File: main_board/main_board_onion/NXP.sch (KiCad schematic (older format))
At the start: 17 parts

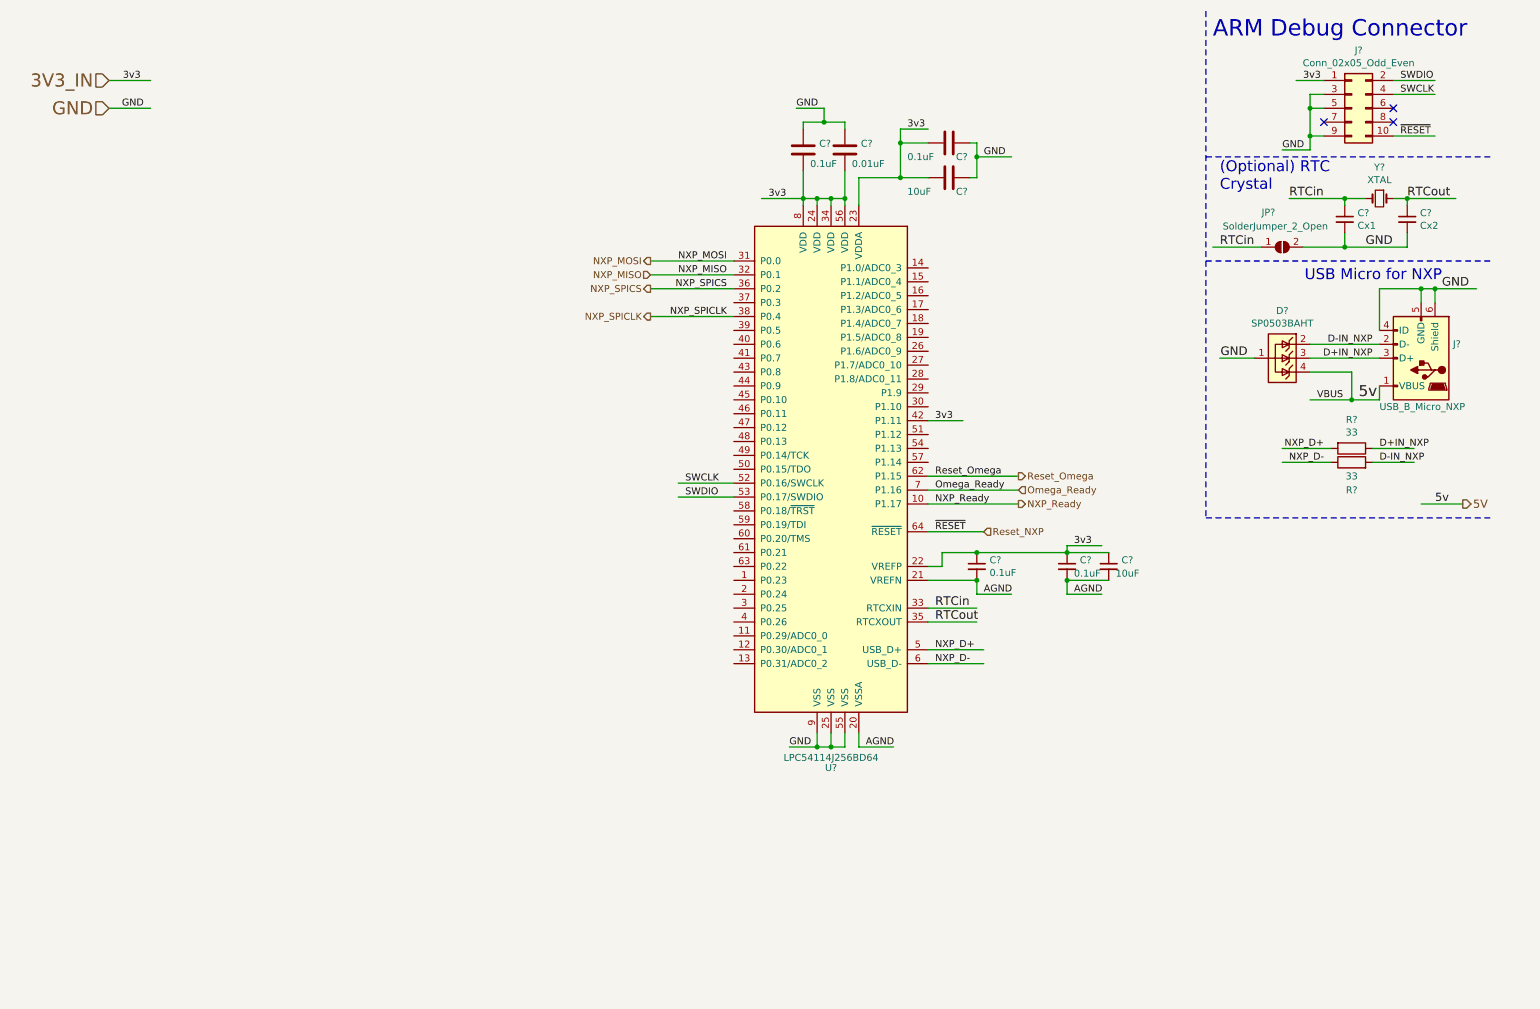
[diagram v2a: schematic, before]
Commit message: Added connectors for sensors
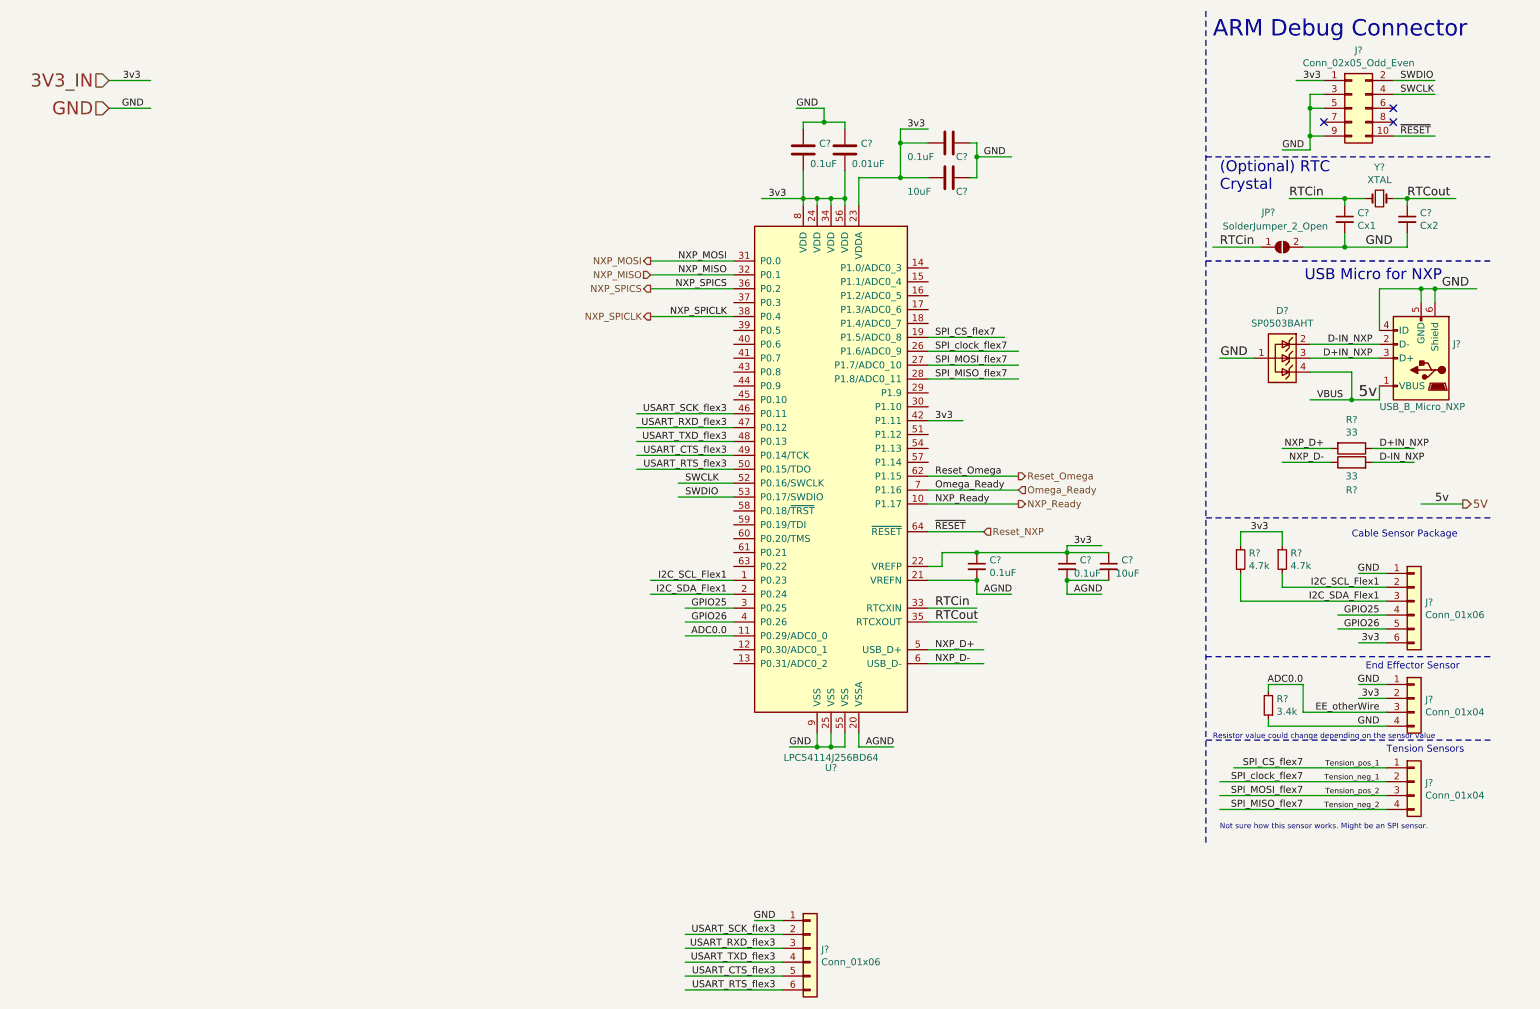
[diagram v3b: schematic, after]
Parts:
- added J? (x2): Conn_01x06, Connector_Molex:Molex_Pico-Lock_504050-0691_1x06-1MP_P1.50mm_Horizontal, symbol Connector_Generic:Conn_01x06
- added J? (x2): Conn_01x04, Connector_Molex:Molex_Pico-Lock_504050-0491_1x04-1MP_P1.50mm_Horizontal, symbol Connector_Generic:Conn_01x04
- added R? (x2): 4.7k, symbol Device:R_Small
- added R?: 3.4k, symbol Device:R_Small
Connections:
- net labels added: ADC0.0, EE_otherWire, GPIO25, GPIO26, I2C_SCL_Flex1, I2C_SDA_Flex1, SPI_CS_flex7, SPI_MISO_flex7, SPI_MOSI_flex7, SPI_clock_flex7, Tension_neg_1, Tension_neg_2, Tension_pos_1, Tension_pos_2, USART_CTS_flex3, USART_RTS_flex3, USART_RXD_flex3, USART_SCK_flex3, USART_TXD_flex3
- wire segments 107 -> 150
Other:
- note added: "Cable Sensor Package"
- note added: "End Effector Sensor"
- note added: "Not sure how this sensor works. Might be an SPI sensor."
- note added: "Resistor value could change depending on the sensor value"
- note added: "Tension Sensors"

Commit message: Linked all schematic symbols to appropriate PCB footprints
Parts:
- C10, C11, C12, C13, C14, C6, C7, C8, C9: renamed from C?; footprint (none) -> Capacitor_SMD:C_0603_1608Metric
- R5, R6, R7, R8, R9: renamed from R?; footprint (none) -> Resistor_SMD:R_0603_1608Metric
- Y1: renamed from Y?; footprint (none) -> Crystal:Crystal_SMD_3215-2Pin_3.2x1.5mm
- gave numbers to parts that had none: 9
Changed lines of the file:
@@
 $EndDescr
 $Comp
-L NXP:LPC54114J256BD64 U?
+L NXP:LPC54114J256BD64 U3
 U 1 1 5B5F9BB3
 P 6450 3800
-F 0 "U?" H 6450 1650 50  0000 C CNN
+F 0 "U3" H 6450 1650 50  0000 C CNN
 F 1 "LPC54114J256BD64" H 6450 1723 50  0000 C CNN
 F 2 "Package_QFP:LQFP-64_10x10mm_P0.5mm" H 7500 5750 50  0001 C CNN
@@
 GND
 $Comp
-L Device:C C?
+L Device:C C6
 U 1 1 5B5F9E20
 P 6250 1500
-F 0 "C?" H 6365 1546 50  0000 L CNN
+F 0 "C6" H 6365 1546 50  0000 L CNN
 F 1 "0.1uF" H 6300 1400 50  0000 L CNN
-F 2 "" H 6288 1350 50  0001 C CNN
+F 2 "Capacitor_SMD:C_0603_1608Metric" H 6288 1350 50  0001 C CNN
 F 3 "~" H 6250 1500 50  0001 C CNN
 	1    6250 1500
@@
 $EndComp
 $Comp
-L Device:C C?
+L Device:C C7
 U 1 1 5B5F9E80
 P 6550 1500
-F 0 "C?" H 6665 1546 50  0000 L CNN
+F 0 "C7" H 6665 1546 50  0000 L CNN
 F 1 "0.01uF" H 6600 1400 50  0000 L CNN
-F 2 "" H 6588 1350 50  0001 C CNN
+F 2 "Capacitor_SMD:C_0603_1608Metric" H 6588 1350 50  0001 C CNN
 F 3 "~" H 6550 1500 50  0001 C CNN
 	1    6550 1500
@@
 GND
 $Comp
-L Device:C C?
+L Device:C C9
 U 1 1 5B5FA2FD
 P 7300 1700
-F 0 "C?" V 7400 1750 50  0000 L CNN
+F 0 "C9" V 7400 1750 50  0000 L CNN
 F 1 "10uF" V 7400 1400 50  0000 L CNN
-F 2 "" H 7338 1550 50  0001 C CNN
+F 2 "Capacitor_SMD:C_0603_1608Metric" H 7338 1550 50  0001 C CNN
 F 3 "~" H 7300 1700 50  0001 C CNN
 	1    7300 1700
@@
 $EndComp
 $Comp
-L Device:C C?
+L Device:C C8
 U 1 1 5B5FA3DF
 P 7300 1450
-F 0 "C?" V 7400 1500 50  0000 L CNN
+F 0 "C8" V 7400 1500 50  0000 L CNN
 F 1 "0.1uF" V 7400 1150 50  0000 L CNN
-F 2 "" H 7338 1300 50  0001 C CNN
+F 2 "Capacitor_SMD:C_0603_1608Metric" H 7338 1300 50  0001 C CNN
 F 3 "~" H 7300 1450 50  0001 C CNN
 	1    7300 1450
@@
 GND
 $Comp
-L Device:C_Small C?
+L Device:C_Small C10
 U 1 1 5B5FAF1A
 P 7500 4500
-F 0 "C?" H 7592 4546 50  0000 L CNN
+F 0 "C10" H 7592 4546 50  0000 L CNN
 F 1 "0.1uF" H 7592 4455 50  0000 L CNN
-F 2 "" H 7500 4500 50  0001 C CNN
+F 2 "Capacitor_SMD:C_0603_1608Metric" H 7500 4500 50  0001 C CNN
 F 3 "~" H 7500 4500 50  0001 C CNN
 	1    7500 4500
@@
 $EndComp
 $Comp
-L Device:C_Small C?
+L Device:C_Small C11
 U 1 1 5B5FB05C
 P 8150 4500
-F 0 "C?" H 8242 4546 50  0000 L CNN
+F 0 "C11" H 8242 4546 50  0000 L CNN
 F 1 "0.1uF" H 8200 4450 50  0000 L CNN
-F 2 "" H 8150 4500 50  0001 C CNN
+F 2 "Capacitor_SMD:C_0603_1608Metric" H 8150 4500 50  0001 C CNN
 F 3 "~" H 8150 4500 50  0001 C CNN
 	1    8150 4500
@@
 $EndComp
 $Comp
-L Device:C_Small C?
+L Device:C_Small C12
 U 1 1 5B5FB0A4
 P 8450 4500
-F 0 "C?" H 8542 4546 50  0000 L CNN
+F 0 "C12" H 8542 4546 50  0000 L CNN
 F 1 "10uF" H 8500 4450 50  0000 L CNN
-F 2 "" H 8450 4500 50  0001 C CNN
+F 2 "Capacitor_SMD:C_0603_1608Metric" H 8450 4500 50  0001 C CNN
 F 3 "~" H 8450 4500 50  0001 C CNN
 	1    8450 4500
@@
 ~RESET
 $Comp
-L Connector_Generic:Conn_02x05_Odd_Even J?
+L Connector_Generic:Conn_02x05_Odd_Even J11
 U 1 1 5B611719
 P 10200 1200
-F 0 "J?" H 10250 1617 50  0000 C CNN
+F 0 "J11" H 10250 1617 50  0000 C CNN
 F 1 "Conn_02x05_Odd_Even" H 10250 1526 50  0000 C CNN
 F 2 "Connector_PinHeader_1.27mm:PinHeader_2x05_P1.27mm_Vertical_SMD" H 10200 1200 50  0001 C CNN
@@
 ARM Debug Connector\n
 $Comp
-L Device:Crystal_Small Y?
+L Device:Crystal_Small Y1
 U 1 1 5B620F7D
 P 10400 1850
-F 0 "Y?" H 10400 1625 50  0000 C CNN
+F 0 "Y1" H 10400 1625 50  0000 C CNN
 F 1 "XTAL" H 10400 1716 50  0000 C CNN
-F 2 "" H 10400 1850 50  0001 C CNN
-F 3 "~" H 10400 1850 50  0001 C CNN
+F 2 "Crystal:Crystal_SMD_3215-2Pin_3.2x1.5mm" H 10400 1850 50  0001 C CNN
+F 3 "https://datasheet.octopart.com/ABS07-120-32.768KHZ-T-Abracon-datasheet-41232047.pdf" H 10400 1850 50  0001 C CNN
 	1    10400 1850
 	-1   0    0    1
 $EndComp
 $Comp
-L Device:C_Small C?
+L Device:C_Small C13
 U 1 1 5B6221AA
 P 10150 2000
-F 0 "C?" H 10242 2046 50  0000 L CNN
+F 0 "C13" H 10242 2046 50  0000 L CNN
 F 1 "Cx1" H 10242 1955 50  0000 L CNN
-F 2 "" H 10150 2000 50  0001 C CNN
+F 2 "Capacitor_SMD:C_0603_1608Metric" H 10150 2000 50  0001 C CNN
 F 3 "~" H 10150 2000 50  0001 C CNN
 	1    10150 2000
@@
 $EndComp
 $Comp
-L Device:C_Small C?
+L Device:C_Small C14
 U 1 1 5B6221EC
 P 10600 2000
-F 0 "C?" H 10692 2046 50  0000 L CNN
+F 0 "C14" H 10692 2046 50  0000 L CNN
 F 1 "Cx2" H 10692 1955 50  0000 L CNN
-F 2 "" H 10600 2000 50  0001 C CNN
+F 2 "Capacitor_SMD:C_0603_1608Metric" H 10600 2000 50  0001 C CNN
 F 3 "~" H 10600 2000 50  0001 C CNN
 	1    10600 2000
@@
 	9150 2300 11200 2300
 $Comp
-L Jumper:SolderJumper_2_Open JP?
+L Jumper:SolderJumper_2_Open JP3
 U 1 1 5B638921
 P 9700 2200
-F 0 "JP?" H 9600 2450 50  0000 C CNN
+F 0 "JP3" H 9600 2450 50  0000 C CNN
 F 1 "SolderJumper_2_Open" H 9650 2350 50  0000 C CNN
 F 2 "Resistor_SMD:R_0805_2012Metric" H 9700 2200 50  0001 C CNN
@@
 RTCin
 $Comp
-L Connector:USB_B_Micro J?
+L Connector:USB_B_Micro J15
 U 1 1 5B63D16B
 P 10700 3000
-F 0 "J?" H 10471 2898 50  0000 R CNN
+F 0 "J15" H 10471 2898 50  0000 R CNN
 F 1 "USB_B_Micro_NXP" H 11000 3350 50  0000 R CNN
 F 2 "Connector_USB:USB_Micro-B_Molex-105017-0001" H 10850 2950 50  0001 C CNN
@@
 Connection ~ 10700 2500
 $Comp
-L Device:R R?
+L Device:R R8
 U 1 1 5B641EBA
 P 10200 3650
-F 0 "R?" V 9993 3650 50  0000 C CNN
+F 0 "R8" V 9993 3650 50  0000 C CNN
 F 1 "33" V 10084 3650 50  0000 C CNN
-F 2 "" V 10130 3650 50  0001 C CNN
+F 2 "Resistor_SMD:R_0603_1608Metric" V 10130 3650 50  0001 C CNN
 F 3 "~" H 10200 3650 50  0001 C CNN
 	1    10200 3650
@@
 $EndComp
 $Comp
-L Device:R R?
+L Device:R R9
 U 1 1 5B641F67
 P 10200 3750
-F 0 "R?" V 10000 3750 50  0000 C CNN
+F 0 "R9" V 10000 3750 50  0000 C CNN
 F 1 "33" V 10100 3750 50  0000 C CNN
-F 2 "" V 10130 3750 50  0001 C CNN
+F 2 "Resistor_SMD:R_0603_1608Metric" V 10130 3750 50  0001 C CNN
 F 3 "~" H 10200 3750 50  0001 C CNN
 	1    10200 3750
@@
 3v3
 $Comp
-L Power_Protection:SP0503BAHT D?
+L Power_Protection:SP0503BAHT D1
 U 1 1 5B678F4C
 P 9700 3000
-F 0 "D?" V 9358 3000 50  0000 C CNN
+F 0 "D1" V 9358 3000 50  0000 C CNN
 F 1 "SP0503BAHT" V 9449 3000 50  0000 C CNN
 F 2 "Package_TO_SOT_SMD:SOT-143" H 9925 2950 50  0001 L CNN
@@
 Reset_Omega
 $Comp
-L Connector_Generic:Conn_01x06 J?
+L Connector_Generic:Conn_01x06 J12
 U 1 1 5B6A4E93
 P 10650 4750
-F 0 "J?" H 10730 4742 50  0000 L CNN
+F 0 "J12" H 10730 4742 50  0000 L CNN
 F 1 "Conn_01x06" H 10730 4651 50  0000 L CNN
 F 2 "Connector_Molex:Molex_Pico-Lock_504050-0691_1x06-1MP_P1.50mm_Horizontal" H 10650 4750 50  0001 C CNN
@@
 	10450 4950 10100 4950
 $Comp
-L Device:R_Small R?
+L Device:R_Small R5
 U 1 1 5B6BE260
 P 9400 4450
-F 0 "R?" H 9459 4496 50  0000 L CNN
+F 0 "R5" H 9459 4496 50  0000 L CNN
 F 1 "4.7k" H 9459 4405 50  0000 L CNN
-F 2 "" H 9400 4450 50  0001 C CNN
+F 2 "Resistor_SMD:R_0603_1608Metric" H 9400 4450 50  0001 C CNN
 F 3 "~" H 9400 4450 50  0001 C CNN
 	1    9400 4450
@@
 $EndComp
 $Comp
-L Device:R_Small R?
+L Device:R_Small R7
 U 1 1 5B6BE322
 P 9700 4450
-F 0 "R?" H 9759 4496 50  0000 L CNN
+F 0 "R7" H 9759 4496 50  0000 L CNN
 F 1 "4.7k" H 9759 4405 50  0000 L CNN
-F 2 "" H 9700 4450 50  0001 C CNN
+F 2 "Resistor_SMD:R_0603_1608Metric" H 9700 4450 50  0001 C CNN
 F 3 "~" H 9700 4450 50  0001 C CNN
 	1    9700 4450
@@
 End Effector Sensor
 $Comp
-L Connector_Generic:Conn_01x04 J?
+L Connector_Generic:Conn_01x04 J13
 U 1 1 5B6ED584
 P 10650 5450
-F 0 "J?" H 10730 5442 50  0000 L CNN
+F 0 "J13" H 10730 5442 50  0000 L CNN
 F 1 "Conn_01x04" H 10730 5351 50  0000 L CNN
 F 2 "Connector_Molex:Molex_Pico-Lock_504050-0491_1x04-1MP_P1.50mm_Horizontal" H 10650 5450 50  0001 C CNN
@@
 	10450 5450 10250 5450
 $Comp
-L Device:R_Small R?
+L Device:R_Small R6
 U 1 1 5B7095E5
 P 9600 5500
-F 0 "R?" H 9541 5454 50  0000 R CNN
+F 0 "R6" H 9541 5454 50  0000 R CNN
 F 1 "3.4k" H 9541 5545 50  0000 R CNN
-F 2 "" H 9600 5500 50  0001 C CNN
+F 2 "Resistor_SMD:R_0603_1608Metric" H 9600 5500 50  0001 C CNN
 F 3 "~" H 9600 5500 50  0001 C CNN
 	1    9600 5500
@@
 Resistor value could change depending on the sensor value
 $Comp
-L Connector_Generic:Conn_01x04 J?
+L Connector_Generic:Conn_01x04 J14
 U 1 1 5B72C26E
 P 10650 6050
-F 0 "J?" H 10730 6042 50  0000 L CNN
+F 0 "J14" H 10730 6042 50  0000 L CNN
 F 1 "Conn_01x04" H 10730 5951 50  0000 L CNN
 F 2 "Connector_Molex:Molex_Pico-Lock_504050-0491_1x04-1MP_P1.50mm_Horizontal" H 10650 6050 50  0001 C CNN
@@
 	5750 3400 5050 3400
 $Comp
-L Connector_Generic:Conn_01x06 J?
+L Connector_Generic:Conn_01x06 J10
 U 1 1 5B7E7861
 P 6300 7250
-F 0 "J?" H 6380 7242 50  0000 L CNN
+F 0 "J10" H 6380 7242 50  0000 L CNN
 F 1 "Conn_01x06" H 6380 7151 50  0000 L CNN
 F 2 "Connector_Molex:Molex_Pico-Lock_504050-0691_1x06-1MP_P1.50mm_Horizontal" H 6300 7250 50  0001 C CNN

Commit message: Added 3d files and placed components on board
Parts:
- J10: value Conn_01x06 -> USART
- J12: value Conn_01x06 -> CableSensor
- J13: value Conn_01x04 -> EndSensor
- J14: value Conn_01x04 -> TensionSensor
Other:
- moved on the sheet: J14
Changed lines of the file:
@@
 P 10650 4750
 F 0 "J12" H 10730 4742 50  0000 L CNN
-F 1 "Conn_01x06" H 10730 4651 50  0000 L CNN
+F 1 "CableSensor" H 10730 4651 50  0000 L CNN
 F 2 "Connector_Molex:Molex_Pico-Lock_504050-0691_1x06-1MP_P1.50mm_Horizontal" H 10650 4750 50  0001 C CNN
 F 3 "~" H 10650 4750 50  0001 C CNN
@@
 GND
 Text Label 10400 5050 2    50   ~ 0
-3v3
+5v
 Text Label 10400 4650 2    50   ~ 0
 I2C_SCL_Flex1
@@
 P 10650 5450
 F 0 "J13" H 10730 5442 50  0000 L CNN
-F 1 "Conn_01x04" H 10730 5351 50  0000 L CNN
+F 1 "EndSensor" H 10730 5351 50  0000 L CNN
 F 2 "Connector_Molex:Molex_Pico-Lock_504050-0491_1x04-1MP_P1.50mm_Horizontal" H 10650 5450 50  0001 C CNN
 F 3 "~" H 10650 5450 50  0001 C CNN
@@
 L Connector_Generic:Conn_01x04 J14
 U 1 1 5B72C26E
-P 10650 6050
-F 0 "J14" H 10730 6042 50  0000 L CNN
-F 1 "Conn_01x04" H 10730 5951 50  0000 L CNN
-F 2 "Connector_Molex:Molex_Pico-Lock_504050-0491_1x04-1MP_P1.50mm_Horizontal" H 10650 6050 50  0001 C CNN
-F 3 "~" H 10650 6050 50  0001 C CNN
-	1    10650 6050
-	1    0    0    -1
-$EndComp
-Text Label 10400 5950 2    39   ~ 0
+P 10600 6050
+F 0 "J14" H 10680 6042 50  0000 L CNN
+F 1 "TensionSensor" H 10680 5951 50  0000 L CNN
+F 2 "Connector_Molex:Molex_Pico-Lock_504050-0491_1x04-1MP_P1.50mm_Horizontal" H 10600 6050 50  0001 C CNN
+F 3 "~" H 10600 6050 50  0001 C CNN
+	1    10600 6050
+	1    0    0    -1
+$EndComp
+Text Label 10350 5950 2    39   ~ 0
 Tension_pos_1
-Text Label 10400 6050 2    39   ~ 0
+Text Label 10350 6050 2    39   ~ 0
 Tension_neg_1
-Text Label 10400 6150 2    39   ~ 0
+Text Label 10350 6150 2    39   ~ 0
 Tension_pos_2
-Text Label 10400 6250 2    39   ~ 0
+Text Label 10350 6250 2    39   ~ 0
 Tension_neg_2
-Text Notes 10450 5850 0    50   ~ 0
+Text Notes 10400 5850 0    50   ~ 0
 Tension Sensors
-Text Notes 9250 6400 0    39   ~ 0
+Text Notes 9200 6400 0    39   ~ 0
 Not sure how this sensor works. Might be an SPI sensor.
 Wire Notes Line
@@
 Wire Wire Line
 	7150 2850 7700 2850
-Text Label 9850 6050 2    50   ~ 0
+Text Label 9800 6050 2    50   ~ 0
 SPI_clock_flex7
-Text Label 9850 6150 2    50   ~ 0
+Text Label 9800 6150 2    50   ~ 0
 SPI_MOSI_flex7
-Text Label 9850 6250 2    50   ~ 0
+Text Label 9800 6250 2    50   ~ 0
 SPI_MISO_flex7
-Text Label 9850 5950 2    50   ~ 0
+Text Label 9800 5950 2    50   ~ 0
 SPI_CS_flex7
 Wire Wire Line
-	9250 6250 10450 6250
-Wire Wire Line
-	9250 6150 10450 6150
-Wire Wire Line
-	9250 6050 10450 6050
-Wire Wire Line
-	9350 5950 10450 5950
+	9200 6250 10400 6250
+Wire Wire Line
+	9200 6150 10400 6150
+Wire Wire Line
+	9200 6050 10400 6050
+Wire Wire Line
+	9300 5950 10400 5950
 Text Label 5700 3500 2    50   ~ 0
 USART_RXD_flex3
@@
 P 6300 7250
 F 0 "J10" H 6380 7242 50  0000 L CNN
-F 1 "Conn_01x06" H 6380 7151 50  0000 L CNN
+F 1 "USART" H 6380 7151 50  0000 L CNN
 F 2 "Connector_Molex:Molex_Pico-Lock_504050-0691_1x06-1MP_P1.50mm_Horizontal" H 6300 7250 50  0001 C CNN
 F 3 "~" H 6300 7250 50  0001 C CNN
